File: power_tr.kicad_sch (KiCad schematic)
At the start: 11 parts, among them J1 DC_2.1mm, Q3 2SC1815, U8 7809, U9 7805

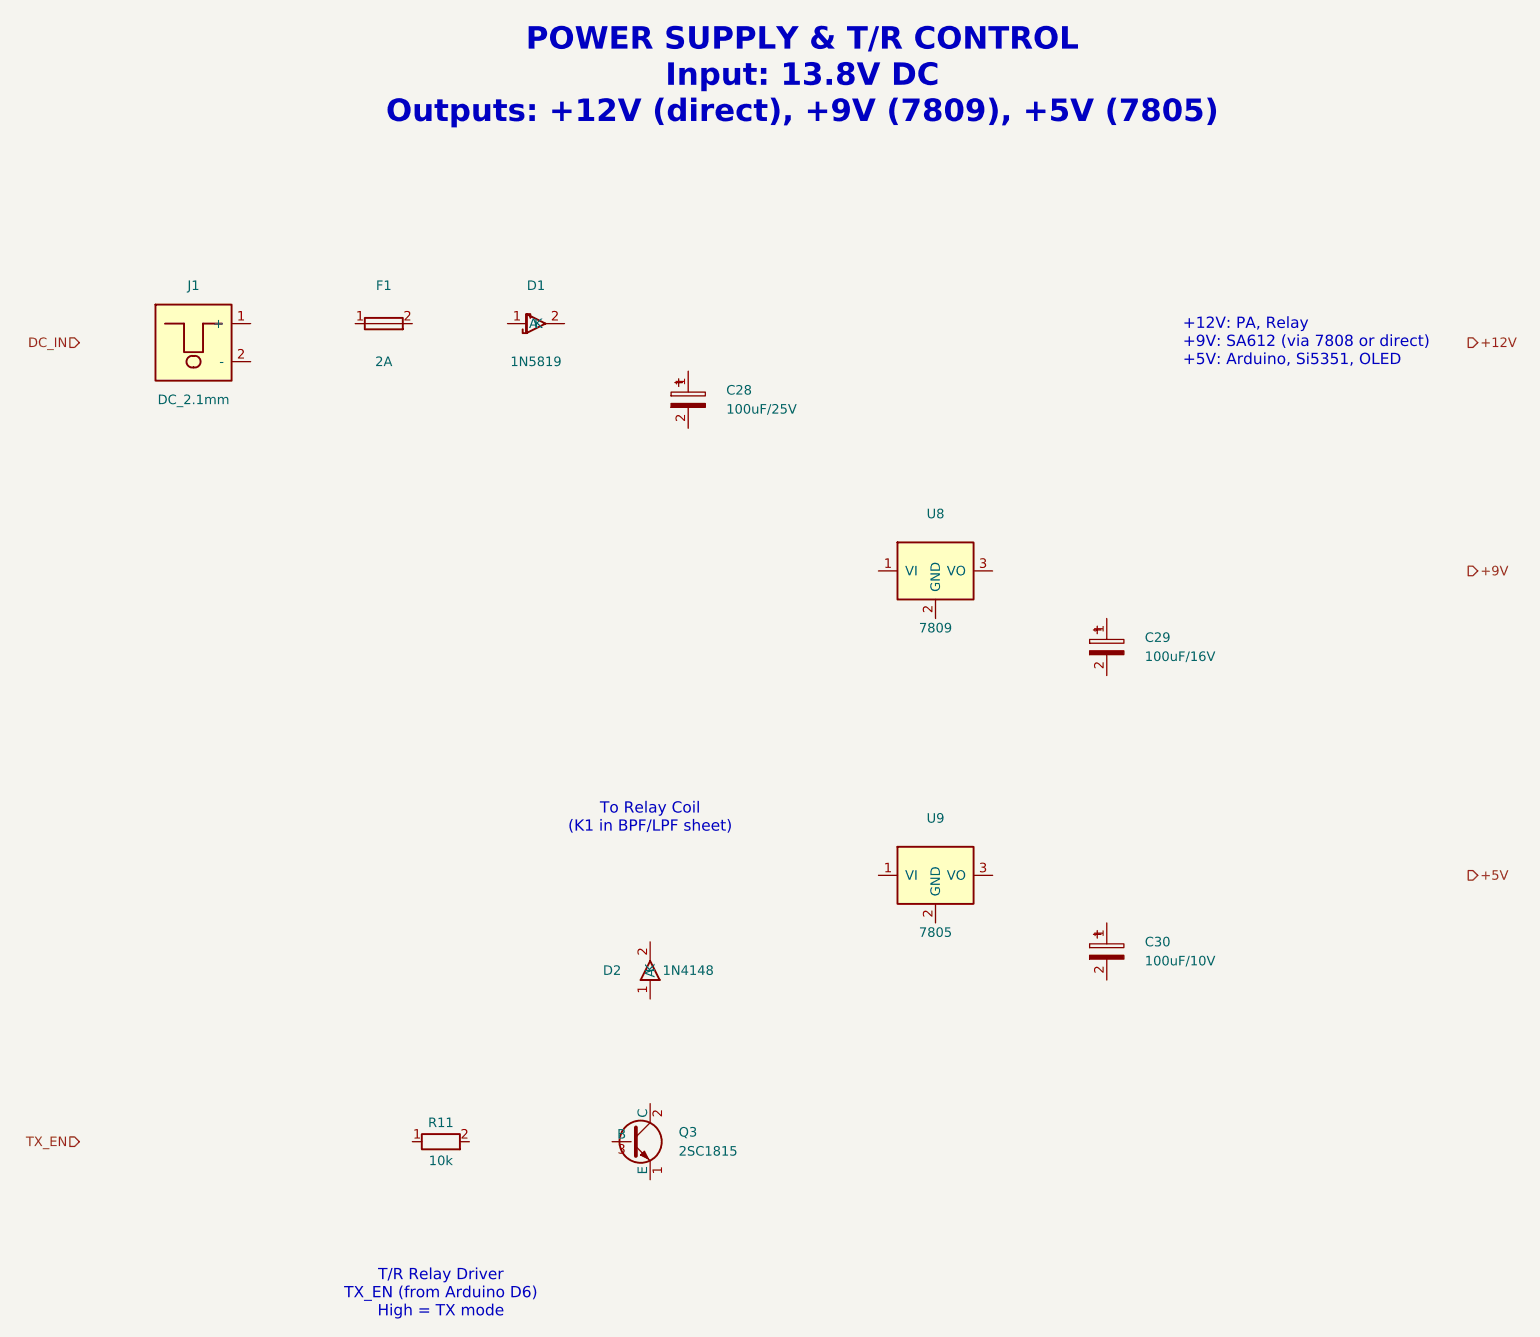
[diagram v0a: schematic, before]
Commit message: Add initial PCB layout with complete component placement
- Create 2-layer PCB (200x100mm) based on KiCad schematic import
- Place all components including Arduino Nano, Si5351, SA612 mixers, SSD1306 OLED
- Position audio amplifier (LM386), voltage regulators (7805/7808), crystal filters
- Add discrete components: resistors, capacitors, inductors, diodes, transistors
- Include connectors for power (DC jack), antenna, speaker, and microphone
- Update .gitignore to exclude fp-info-cache and backup directories
- Update schematic symbols for all circuit blocks (audio, BPF/LPF, control, IF filter, mixer/modulator, power amp, power supply)
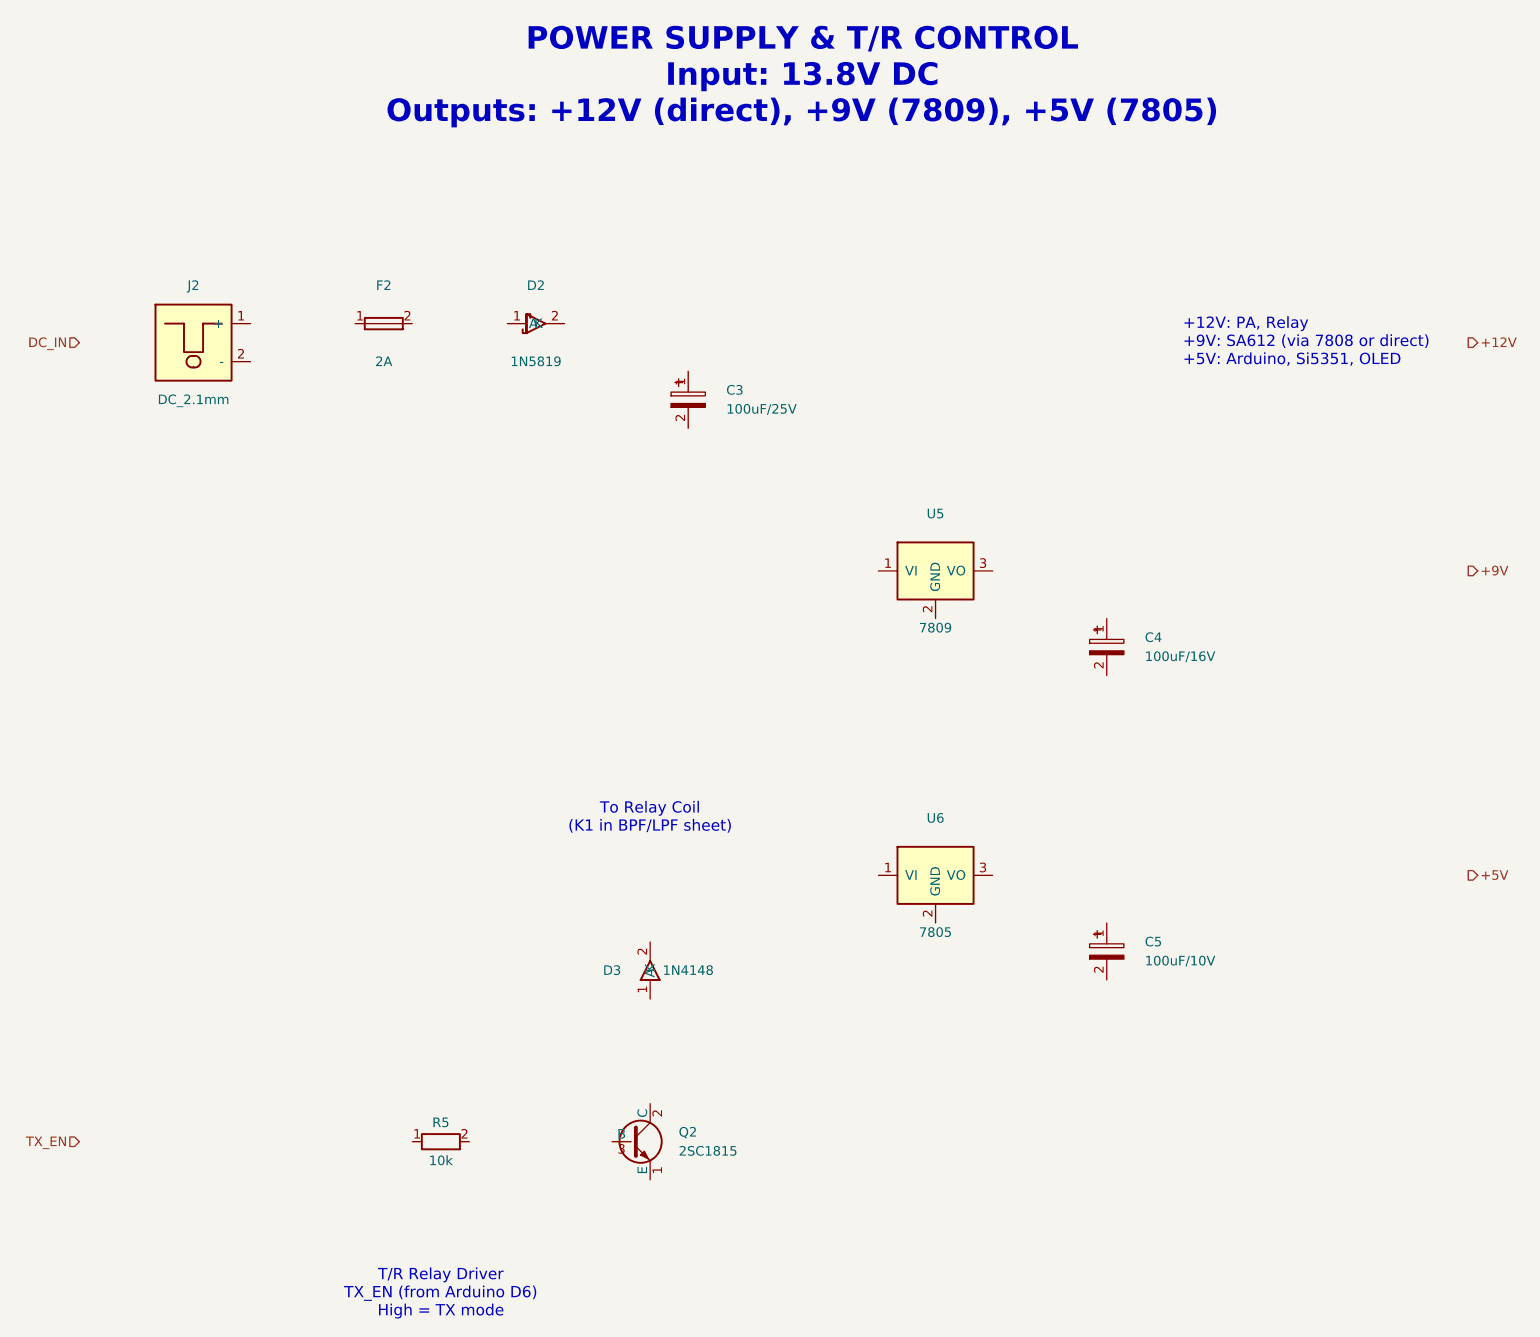
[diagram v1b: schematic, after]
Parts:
- removed C28: 100uF/25V, symbol Device:CP
- removed C29: 100uF/16V, symbol Device:CP
- removed C30: 100uF/10V, symbol Device:CP
- removed D1: 1N5819, symbol Device:D_Schottky
- removed D2: 1N4148, symbol Device:D
- removed F1: 2A, symbol Device:Fuse
- removed J1: DC_2.1mm, symbol Connector:DC_Jack
- removed Q3: 2SC1815, symbol Transistor:2SC1815
- removed R11: 10k, symbol Device:R
- removed U8: 7809, symbol Regulator:7809
- removed U9: 7805, symbol Regulator:7805
- added C3: 100uF/25V, Capacitor_THT:CP_Radial_D5.0mm_P2.50mm, symbol Device:CP
- added C4: 100uF/16V, Capacitor_THT:CP_Radial_D5.0mm_P2.50mm, symbol Device:CP
- added C5: 100uF/10V, Capacitor_THT:CP_Radial_D5.0mm_P2.50mm, symbol Device:CP
- added D2: 1N5819, Diode_THT:D_DO-35_SOD27_P7.62mm_Horizontal, symbol Device:D_Schottky
- added D3: 1N4148, Diode_THT:D_DO-35_SOD27_P7.62mm_Horizontal, symbol Device:D
- added F2: 2A, Fuse:Fuseholder_Cylinder-5x20mm_Schurter_0031_8201_Horizontal_Open, symbol Device:Fuse
- added J2: DC_2.1mm, Connector_BarrelJack:BarrelJack_Horizontal, symbol Connector:DC_Jack
- added Q2: 2SC1815, Package_TO_SOT_THT:TO-92_Inline, symbol Transistor:2SC1815
- added R5: 10k, Resistor_THT:R_Axial_DIN0207_L6.3mm_D2.5mm_P10.16mm_Horizontal, symbol Device:R
- added U5: 7809, Package_TO_SOT_THT:TO-220-3_Vertical, symbol Regulator:7809
- added U6: 7805, Package_TO_SOT_THT:TO-220-3_Vertical, symbol Regulator:7805
